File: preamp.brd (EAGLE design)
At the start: 101.6 x 100 mm, 78 parts, among them IC1 OPAMP-QUADTL074, IC2 OPAMP-QUADTL074, IC3 OPAMP-DUALDIP, IC7 OPAMP-QUADTL074, J1 Instrument Input, J2 Instrument Output, SW1 SWITCH_DPDT

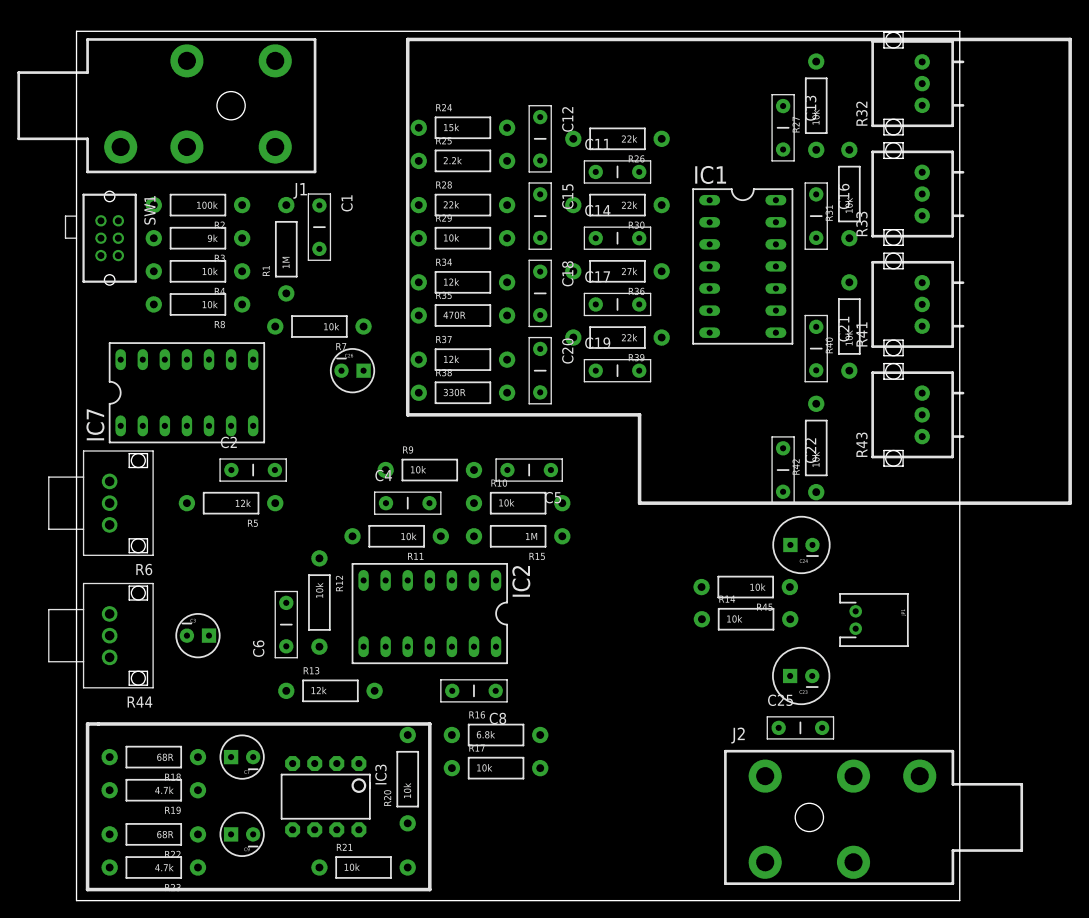
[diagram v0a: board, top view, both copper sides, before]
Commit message: updated board size
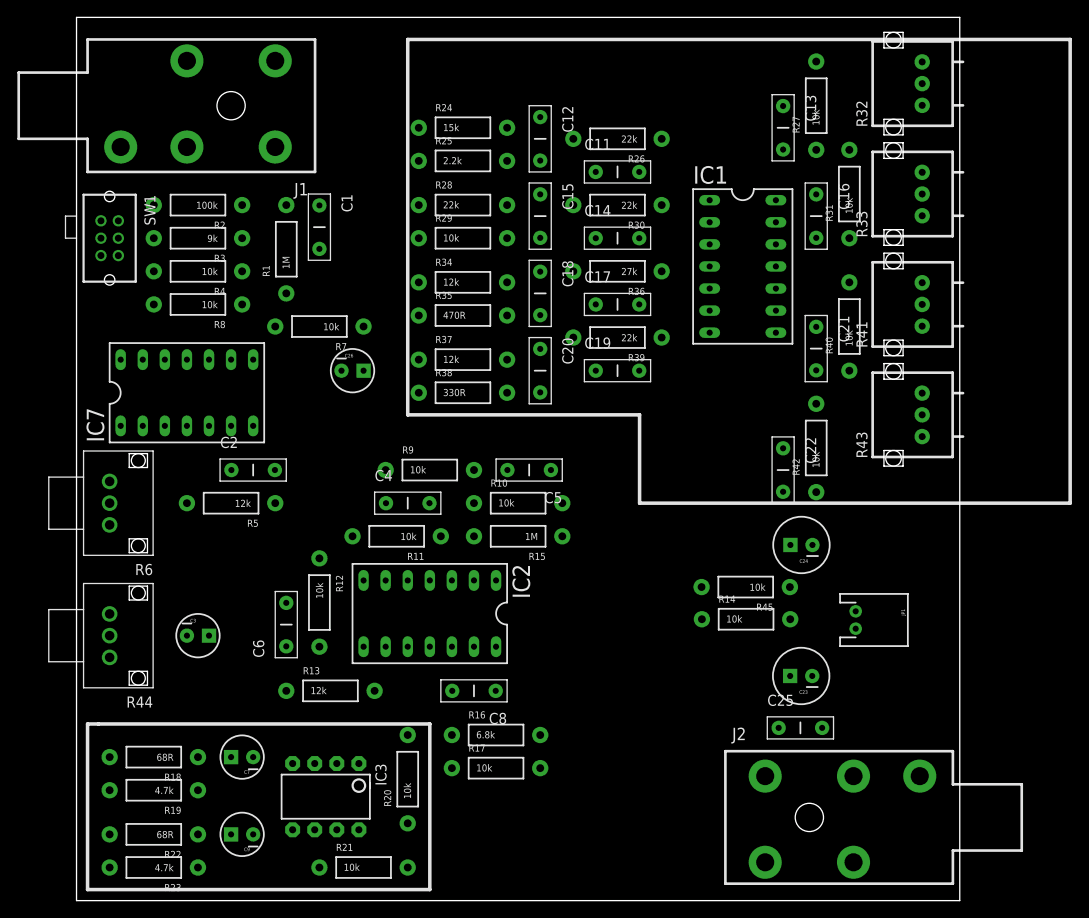
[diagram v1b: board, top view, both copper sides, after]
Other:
- board size 101.6 x 100 mm -> 101.6 x 101.6 mm
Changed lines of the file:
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@@
 <plain>
 <wire x1="0" y1="0" x2="101.6" y2="0" width="0" layer="20"/>
-<wire x1="101.6" y1="0" x2="101.6" y2="100" width="0" layer="20"/>
-<wire x1="101.6" y1="100" x2="0" y2="100" width="0" layer="20"/>
-<wire x1="0" y1="100" x2="0" y2="0" width="0" layer="20"/>
+<wire x1="101.6" y1="0" x2="101.6" y2="101.6" width="0" layer="20"/>
+<wire x1="101.6" y1="101.6" x2="0" y2="101.6" width="0" layer="20"/>
+<wire x1="0" y1="101.6" x2="0" y2="0" width="0" layer="20"/>
 <wire x1="38.1" y1="99.06" x2="114.3" y2="99.06" width="0.4064" layer="21"/>
 <wire x1="114.3" y1="99.06" x2="114.3" y2="45.72" width="0.4064" layer="21"/>
